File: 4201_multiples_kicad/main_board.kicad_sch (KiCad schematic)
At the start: 29 parts, among them J17 Conn_02x05_Odd_Even, U1 TL074, U2 TL074

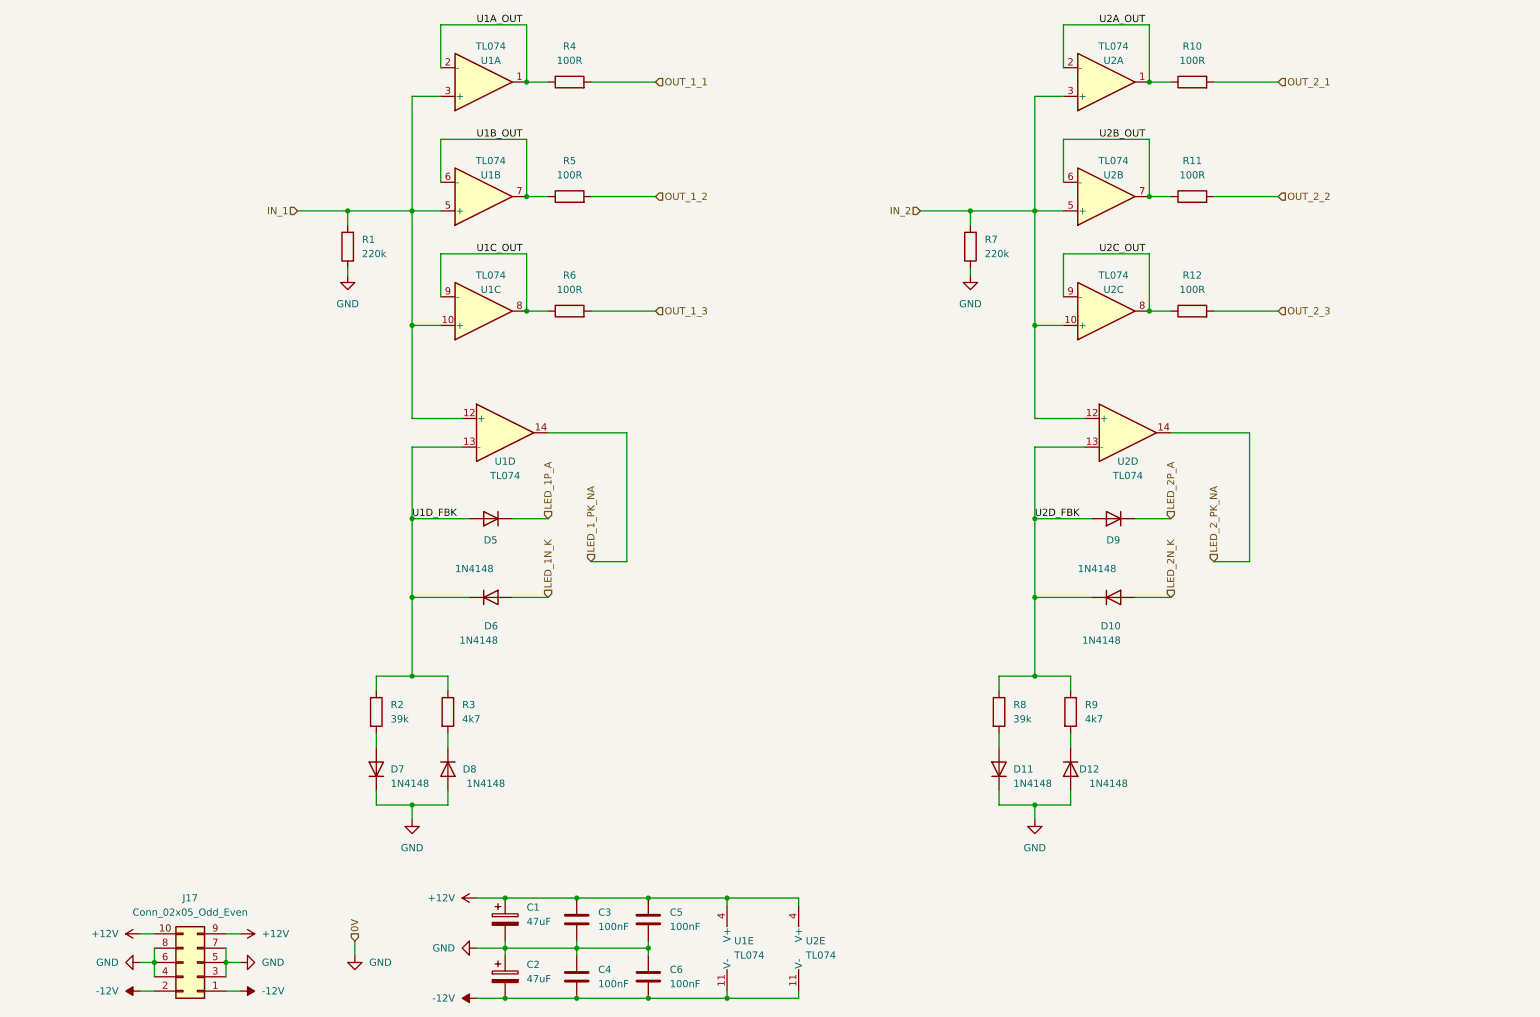
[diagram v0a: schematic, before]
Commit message: Finish layout first draft
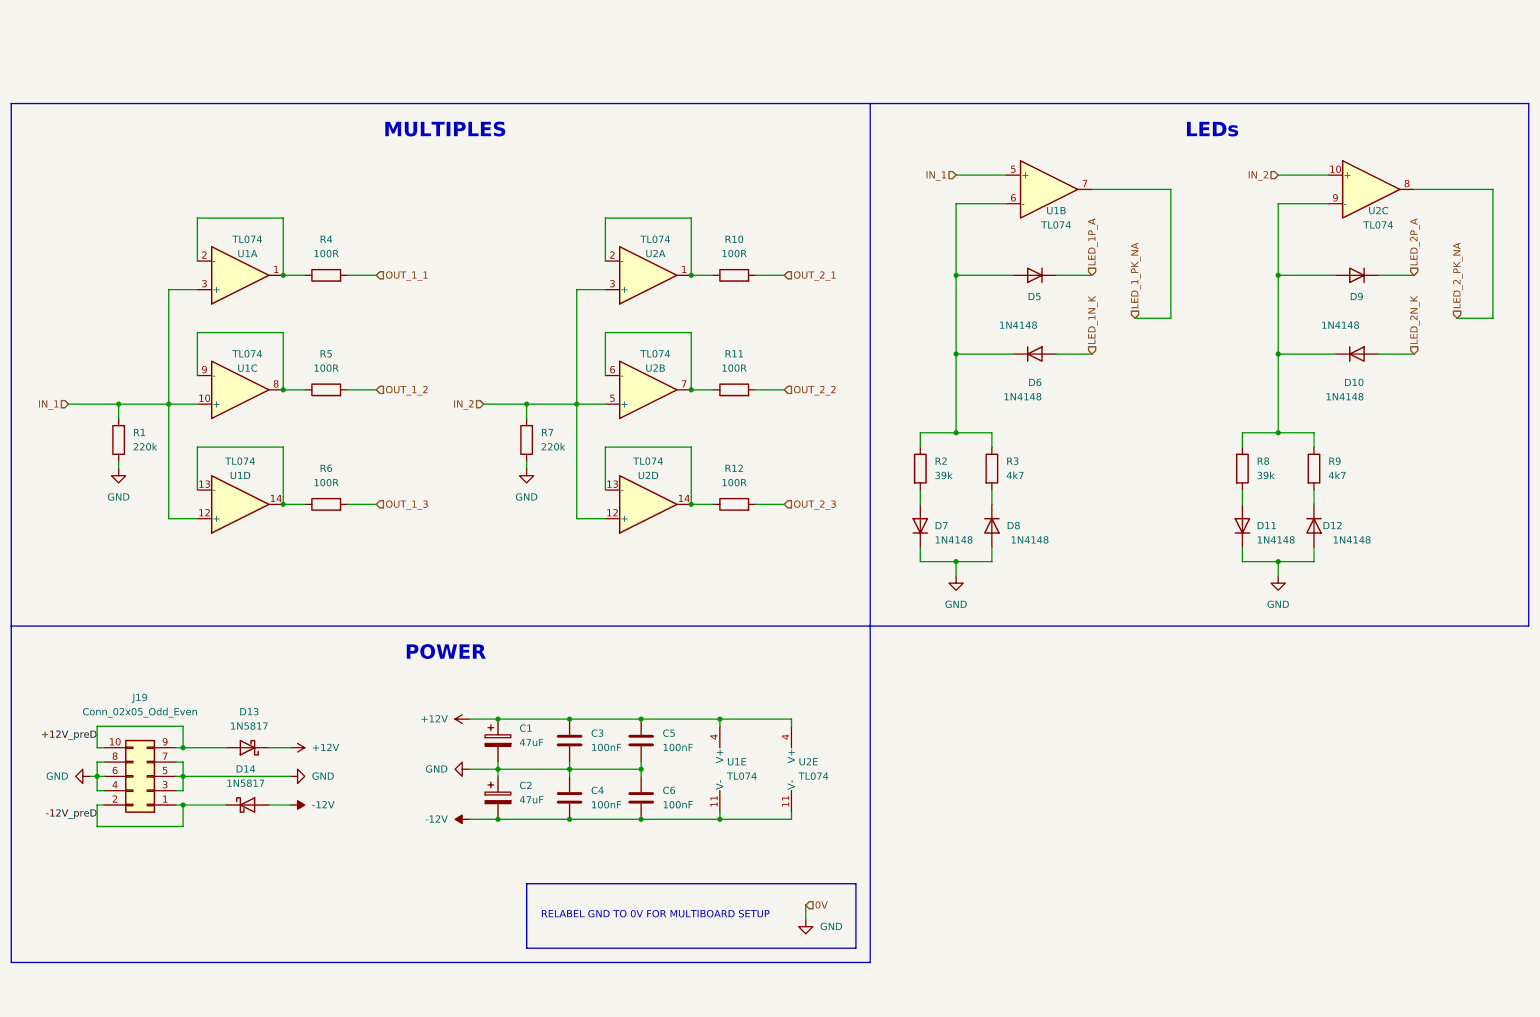
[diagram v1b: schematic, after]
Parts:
- added D13, D14: 1N5817, Diode_SMD:D_1206_3216Metric_Pad1.42x1.75mm_HandSolder, symbol Diode:1N5817
- renumbered J17 to J19
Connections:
- net +12V: now also D13.1 (K); no longer J19.10 (Pin_10), J19.9 (Pin_9)
- net -12V: now also D14.2 (A); no longer J19.1 (Pin_1), J19.2 (Pin_2)
- net LED_1_PK_NA: now also U1.7; no longer U1.14
- net LED_2_PK_NA: now also U2.8; no longer U2.14
- net U1A_OUT: no longer names the net of R4.1, U1.1, U1.2 (-)
- removed net U1B_OUT: R5.1, U1.6 (-), U1.7
- net U1C_OUT: no longer names the net of U1.8, U1.9 (-)
- net U1C_OUT: now also R5.1; no longer R6.1
- net U1D_FBK: no longer names the net of D5.2 (A), D6.1 (K), R2.1, R3.1
- net U1D_FBK: now also U1.6 (-); no longer U1.13 (-)
- net U2A_OUT: no longer names the net of R10.1, U2.1, U2.2 (-)
- net U2B_OUT: no longer names the net of R11.1, U2.6 (-), U2.7
- removed net U2C_OUT: R12.1, U2.8, U2.9 (-)
- net U2D_FBK: no longer names the net of D10.1 (K), D9.2 (A), R8.1, R9.1
- net U2D_FBK: now also U2.9 (-); no longer U2.13 (-)
- new net: R12.1, U2.13 (-), U2.14
- new net: R6.1, U1.13 (-), U1.14
- new net +12V_preD: D13.2 (A), J19.10 (Pin_10), J19.9 (Pin_9)
- new net -12V_preD: D14.1 (K), J19.1 (Pin_1), J19.2 (Pin_2)
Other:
- note added: "LEDs"
- note added: "MULTIPLES"
- note added: "POWER"
- note added: "RELABEL GND TO 0V FOR MULTIBOARD SETUP"
- moved on the sheet: C1, C2, C3, C4, C5, C6, D10, D11, D12, D5, D6, D7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

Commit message: Small touches
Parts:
- D13, D14: value 1N5817 -> Schottky
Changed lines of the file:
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@@
     (in_bom yes) (on_board yes) (fields_autoplaced)
     (property "Reference" "D13" (id 0) (at 56.1975 139.7 0))
-    (property "Value" "1N5817" (id 1) (at 56.1975 142.24 0))
+    (property "Value" "Schottky" (id 1) (at 56.1975 142.24 0))
     (property "Footprint" "Diode_SMD:D_1206_3216Metric_Pad1.42x1.75mm_HandSolder" (id 2) (at 55.88 141.605 0)
       (effects (font (size 1.27 1.27)) hide)
@@
     (in_bom yes) (on_board yes) (fields_autoplaced)
     (property "Reference" "D14" (id 0) (at 55.5625 149.86 0))
-    (property "Value" "1N5817" (id 1) (at 55.5625 152.4 0))
+    (property "Value" "Schottky" (id 1) (at 55.5625 152.4 0))
     (property "Footprint" "Diode_SMD:D_1206_3216Metric_Pad1.42x1.75mm_HandSolder" (id 2) (at 55.88 160.655 0)
       (effects (font (size 1.27 1.27)) hide)

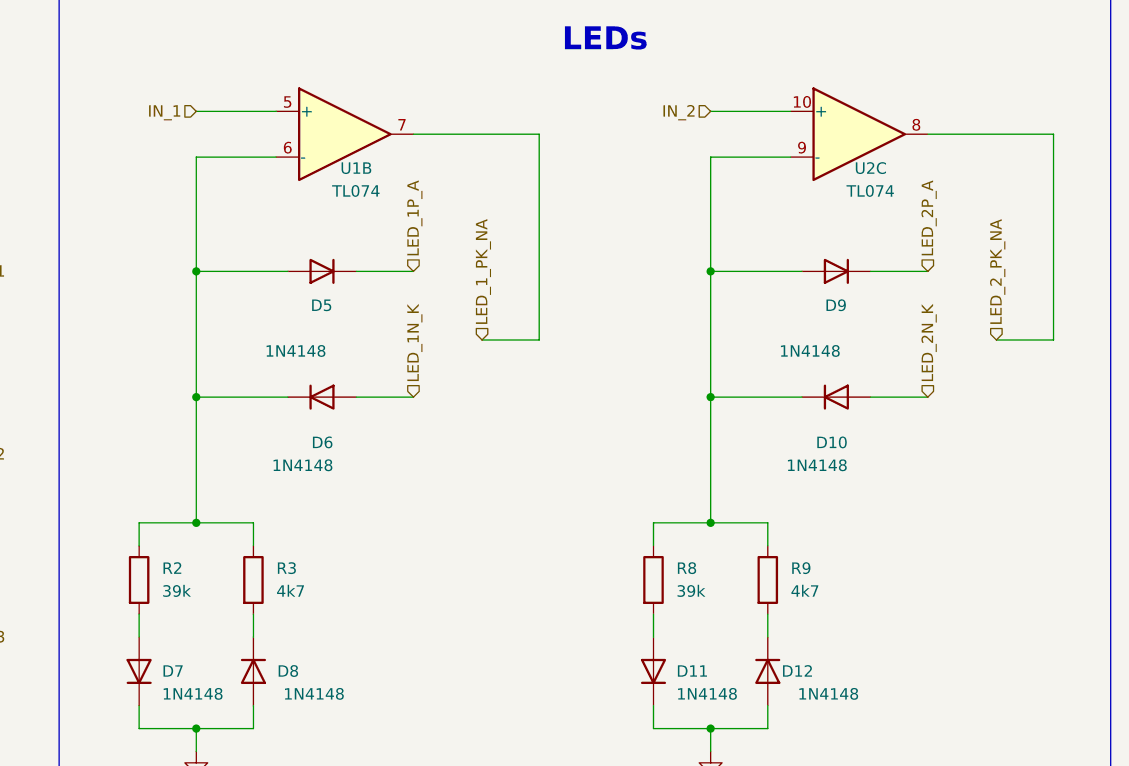
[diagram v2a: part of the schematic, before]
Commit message: Add stitching vias and clean up files
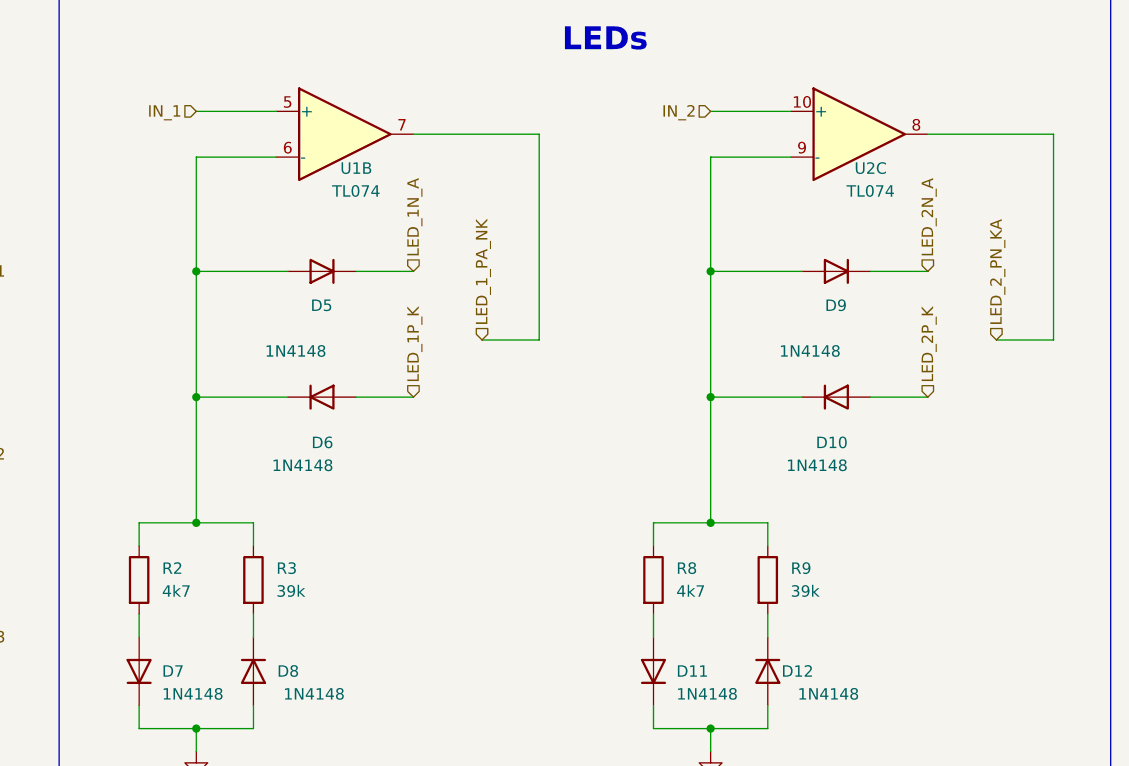
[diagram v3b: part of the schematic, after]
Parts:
- R2, R8: value 39k -> 4k7
- R3, R9: value 4k7 -> 39k
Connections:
- net LED_1N_K renamed LED_1P_K
- net LED_1P_A renamed LED_1N_A
- net LED_1_PK_NA renamed LED_1_PA_NK
- net LED_2N_K renamed LED_2P_K
- net LED_2P_A renamed LED_2N_A
- net LED_2_PK_NA renamed LED_2_PN_KA
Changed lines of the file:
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@@
     (effects (font (size 1.27 1.27)) (justify left))
   )
-  (hierarchical_label "LED_2_PK_NA" (shape input) (at 270.51 69.85 90)
+  (hierarchical_label "LED_2_PN_KA" (shape input) (at 270.51 69.85 90)
     (effects (font (size 1.27 1.27)) (justify left))
   )
@@
     (effects (font (size 1.27 1.27)) (justify left))
   )
-  (hierarchical_label "LED_2P_A" (shape input) (at 262.89 62.23 90)
-    (effects (font (size 1.27 1.27)) (justify left))
-  )
-  (hierarchical_label "LED_1_PK_NA" (shape input) (at 213.36 69.85 90)
-    (effects (font (size 1.27 1.27)) (justify left))
-  )
-  (hierarchical_label "LED_1P_A" (shape input) (at 205.74 62.23 90)
+  (hierarchical_label "LED_2N_A" (shape input) (at 262.89 62.23 90)
+    (effects (font (size 1.27 1.27)) (justify left))
+  )
+  (hierarchical_label "LED_1_PA_NK" (shape input) (at 213.36 69.85 90)
+    (effects (font (size 1.27 1.27)) (justify left))
+  )
+  (hierarchical_label "LED_1N_A" (shape input) (at 205.74 62.23 90)
     (effects (font (size 1.27 1.27)) (justify left))
   )
@@
     (effects (font (size 1.27 1.27)) (justify left))
   )
-  (hierarchical_label "LED_2N_K" (shape input) (at 262.89 76.2 90)
+  (hierarchical_label "LED_2P_K" (shape input) (at 262.89 76.2 90)
     (effects (font (size 1.27 1.27)) (justify left))
   )
@@
     (effects (font (size 1.27 1.27)) (justify left))
   )
-  (hierarchical_label "LED_1N_K" (shape input) (at 205.74 76.2 90)
+  (hierarchical_label "LED_1P_K" (shape input) (at 205.74 76.2 90)
     (effects (font (size 1.27 1.27)) (justify left))
   )
@@
       (effects (font (size 1.27 1.27)) (justify left))
     )
-    (property "Value" "4k7" (id 1) (at 190.5 97.7899 0)
+    (property "Value" "39k" (id 1) (at 190.5 97.7899 0)
       (effects (font (size 1.27 1.27)) (justify left))
     )
@@
       (effects (font (size 1.27 1.27)) (justify left))
     )
-    (property "Value" "39k" (id 1) (at 234.95 97.7899 0)
+    (property "Value" "4k7" (id 1) (at 234.95 97.7899 0)
       (effects (font (size 1.27 1.27)) (justify left))
     )
@@
       (effects (font (size 1.27 1.27)) (justify left))
     )
-    (property "Value" "4k7" (id 1) (at 247.65 97.7899 0)
+    (property "Value" "39k" (id 1) (at 247.65 97.7899 0)
       (effects (font (size 1.27 1.27)) (justify left))
     )
@@
       (effects (font (size 1.27 1.27)) (justify left))
     )
-    (property "Value" "39k" (id 1) (at 177.8 97.7899 0)
-      (effects (font (size 1.27 1.27)) (justify left))
-    )
+    (property "Value" "4k7" (id 1) (at 177.8 97.7899 0)
+      (effects (font (size 1.27 1.27)) (justify left))
+    )

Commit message: Small changes, cleanup
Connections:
- net at R3.2: now also D7.2 (A); no longer D8.1 (K)
- net at D11.2 (A): now also R9.2; no longer R8.2
- net at D12.1 (K): now also R8.2; no longer R9.2
- net at R2.2: now also D8.1 (K); no longer D7.2 (A)
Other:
- moved on the sheet: D10, D5, D6, D9, R2, R3, R8, R9
